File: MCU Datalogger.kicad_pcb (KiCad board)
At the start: 2 copper layers, 0 parts

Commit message: Setup Pcbnew.
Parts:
- added BT1: Battery, Connector_PinHeader_2.54mm:PinHeader_1x02_P2.54mm_Vertical, F.Cu at (227.9, 113.7)
- added C1: 0.1uF, Capacitor_SMD:C_0805_2012Metric, F.Cu at (250.2, 103.4)
- added C2: 22pF, Capacitor_SMD:C_0805_2012Metric, F.Cu at (250.2, 106.4)
- added C3: 22pF, Capacitor_SMD:C_0805_2012Metric, F.Cu at (250.2, 109.4)
- added C4: 0.1uF, Capacitor_SMD:C_0805_2012Metric, F.Cu at (250.2, 112.4)
- added C5: 100nF, Capacitor_SMD:C_0805_2012Metric, F.Cu at (250.2, 115.5)
- added D1: LED, LED_SMD:LED_0805_2012Metric, F.Cu at (254.7, 103.4)
- added D2: LED, LED_SMD:LED_0805_2012Metric, F.Cu at (254.7, 106.5)
- added H1: MountingHole, MountingHole:MountingHole_2.1mm, F.Cu at (228.5, 91.2)
- added H2: MountingHole, MountingHole:MountingHole_2.1mm, F.Cu at (228.5, 97.0)
- added H3: MountingHole, MountingHole:MountingHole_2.1mm, F.Cu at (228.5, 102.7)
- added H4: MountingHole, MountingHole:MountingHole_2.1mm, F.Cu at (228.5, 108.5)
- added J1: Conn_01x04_Pin, Connector_PinHeader_2.54mm:PinHeader_1x04_P2.54mm_Vertical, F.Cu at (265.9, 90.7)
- added J2: Conn_01x09_Pin, Connector_PinHeader_2.54mm:PinHeader_1x09_P2.54mm_Vertical, F.Cu at (261.2, 90.7)
- added J3: Conn_01x04_Pin, Connector_PinHeader_2.54mm:PinHeader_1x04_P2.54mm_Vertical, F.Cu at (270.5, 90.7)
- added J4: Conn_02x03_Odd_Even, Connector_PinHeader_2.54mm:PinHeader_2x03_P2.54mm_Vertical, F.Cu at (265.9, 102.9)
- added R1: 10K, Resistor_SMD:R_0805_2012Metric, F.Cu at (233.6, 89.8)
- added R2: 10K, Resistor_SMD:R_0805_2012Metric, F.Cu at (233.6, 92.8)
- added R3: 4.7K, Resistor_SMD:R_0805_2012Metric, F.Cu at (233.6, 95.7)
- added R4: 4.7K, Resistor_SMD:R_0805_2012Metric, F.Cu at (233.6, 98.7)
- added R5: 330, Resistor_SMD:R_0805_2012Metric, F.Cu at (233.6, 101.6)
- added R6: 10K, Resistor_SMD:R_0805_2012Metric, F.Cu at (233.6, 104.6)
- added R7: 330, Resistor_SMD:R_0805_2012Metric, F.Cu at (233.6, 107.5)
- added U1: 24LC1025, Package_SO:SOIC-8_5.23x5.23mm_P1.27mm, F.Cu at (240.9, 91.8)
- added U2: DS1337S_, Footprints:SOIC127P600X175-8N, F.Cu at (240.9, 116.5)
- added U3: 24LC1025, Package_SO:SOIC-8_5.23x5.23mm_P1.27mm, F.Cu at (240.9, 98.5)
- added U4: ATMEGA328P-AU, Footprints:QFP80P900X900X120-32N, F.Cu at (242.3, 107.6)
- added Y1: 32.768 KHz, Crystal:Crystal_SMD_5032-2Pin_5.0x3.2mm_HandSoldering, F.Cu at (251.2, 90.8)
- added Y2: 16 MHz, Crystal:Crystal_SMD_5032-2Pin_5.0x3.2mm_HandSoldering, F.Cu at (251.2, 95.6)

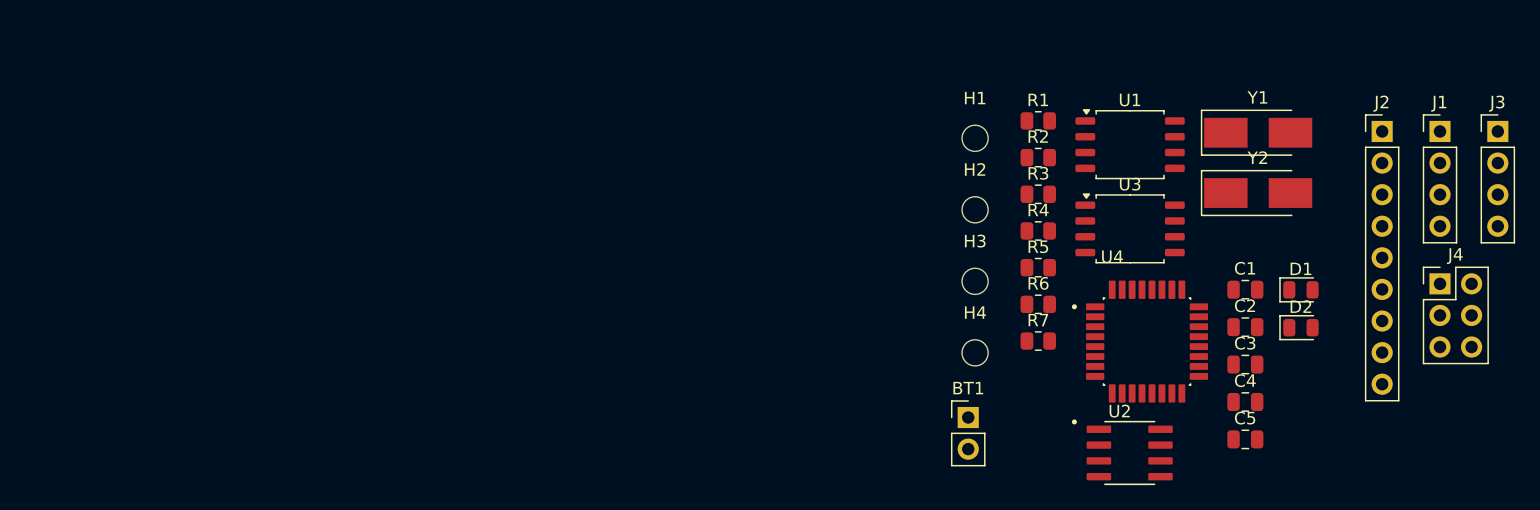
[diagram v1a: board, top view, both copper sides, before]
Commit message: Completed placement of footprints.
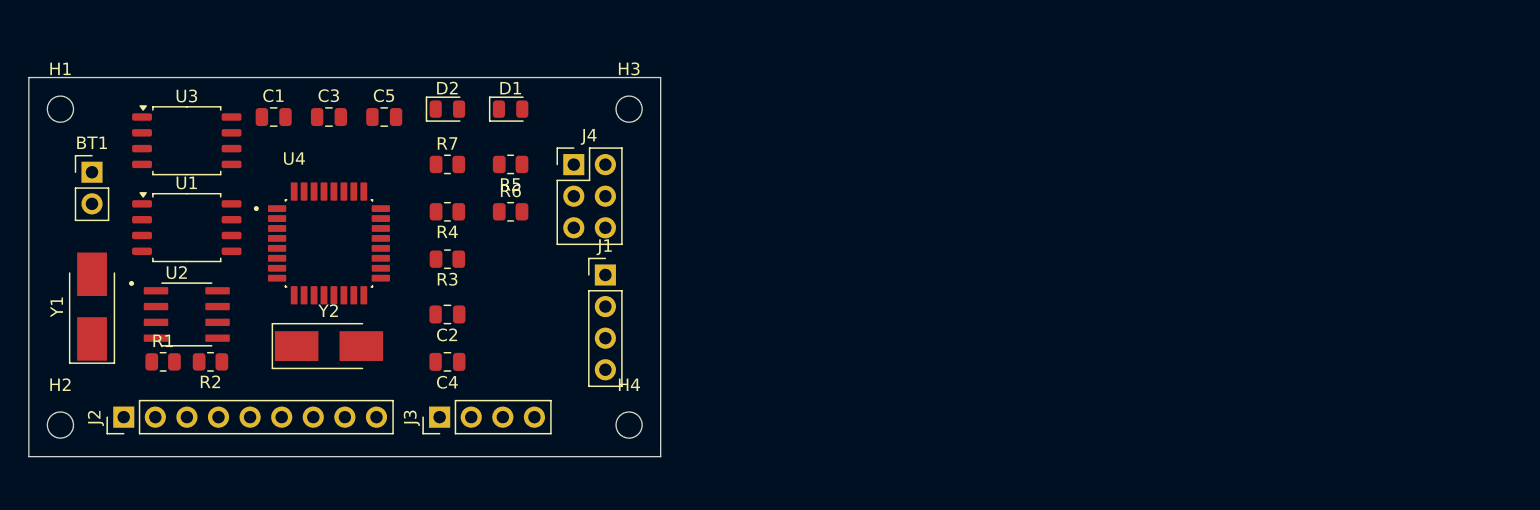
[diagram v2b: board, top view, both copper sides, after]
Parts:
- moved J2 103.8 mm to (160.0, 113.7), turned to 90 degrees
- moved Y1 94.8 mm to (157.5, 104.8), turned to 90 degrees
- moved J3 88.1 mm to (185.4, 113.7), turned to 90 degrees
- moved C1 79.4 mm to (172.1, 89.5)
- moved U2 76.6 mm to (165.1, 105.4)
- moved C3 76.3 mm to (176.5, 89.5)
- moved U3 76.2 mm to (165.1, 91.4)
- moved U1 76.1 mm to (165.1, 98.4)
- moved Y2 75.7 mm to (176.5, 108.0)
- moved H2 75.6 mm to (154.9, 114.3)
- moved C5 73.9 mm to (181.0, 89.5)
- moved H1 73.6 mm to (154.9, 88.9)
- moved BT1 73.2 mm to (157.5, 94.0)
- moved R1 73.0 mm to (163.2, 109.2)
- moved D2 70.8 mm to (186.1, 88.9)
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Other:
- board outline added: 50.8 x 30.5 mm

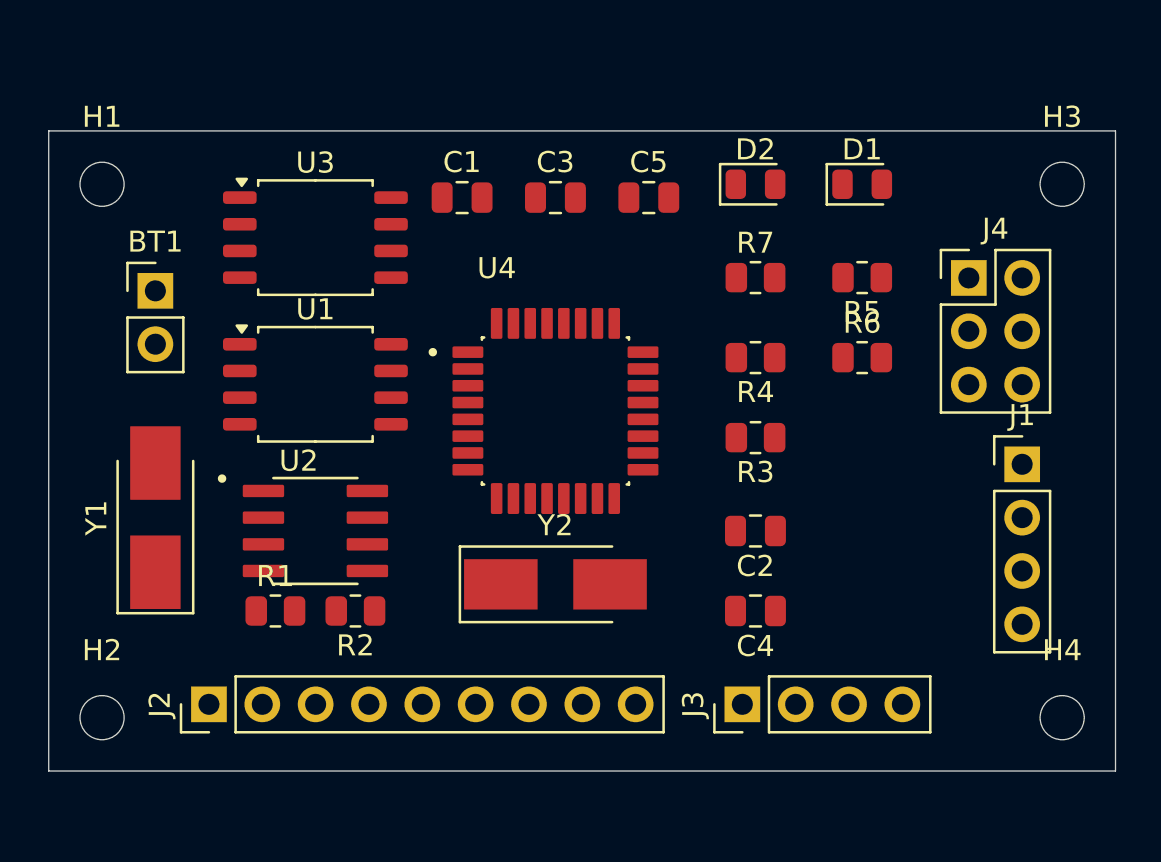
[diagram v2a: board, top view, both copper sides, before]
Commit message: Redesigned board shape.
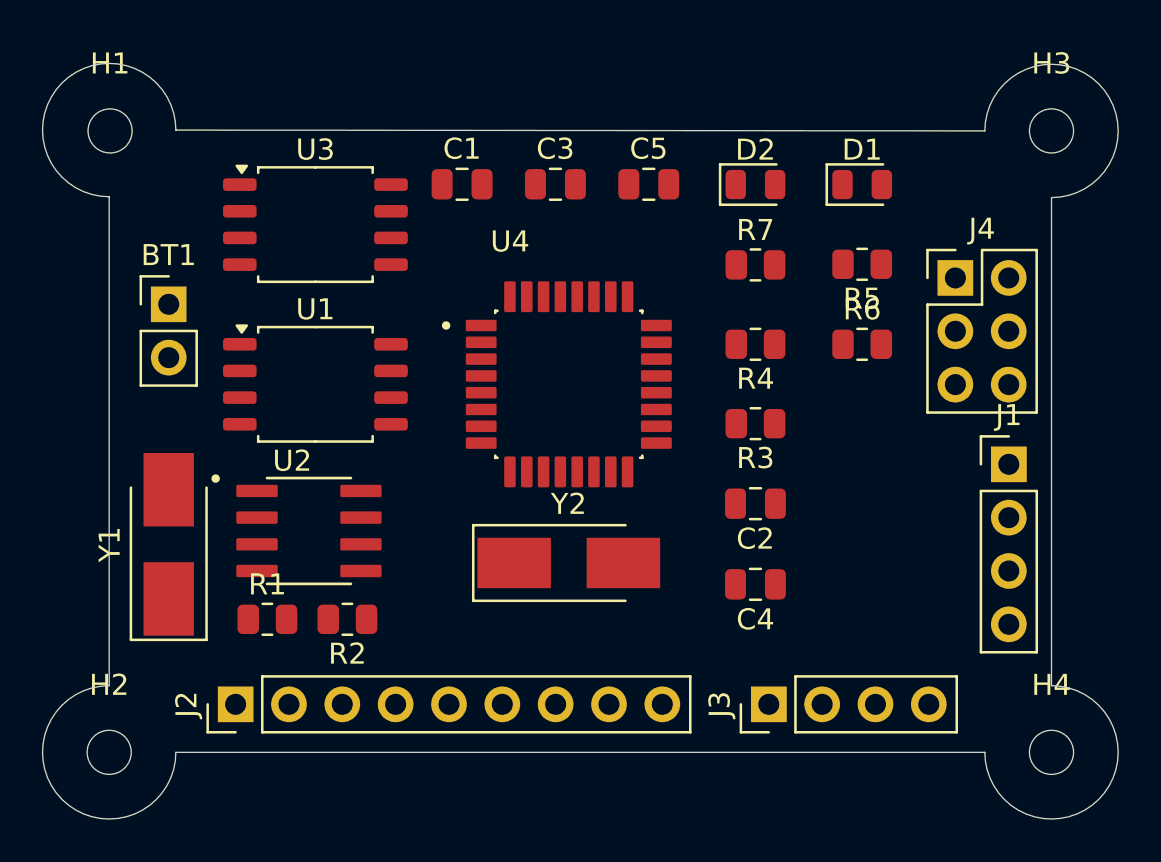
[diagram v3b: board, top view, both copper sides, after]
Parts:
- moved H3 2.59 mm to (200.2, 86.4)
- moved H1 2.57 mm to (155.3, 86.4)
- moved H4 1.73 mm to (200.2, 116.0)
- moved H2 1.69 mm to (155.3, 116.0)
- moved Y1 1.42 mm to (158.1, 106.0)
- moved U4 1.42 mm to (177.2, 98.4)
- moved C2 1.30 mm to (186.1, 104.1)
- moved J2 1.27 mm to (161.3, 113.7)
- moved C4 1.27 mm to (186.1, 108.0)
- moved J3 1.26 mm to (186.7, 113.7)
- moved Y2 1.20 mm to (177.2, 106.9)
- moved BT1 0.90 mm to (158.1, 94.6)
- moved R3 0.67 mm to (186.1, 100.3)
- moved J4 0.64 mm to (195.6, 93.4)
- moved R4 0.64 mm to (186.1, 96.5)
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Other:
- board size 50.8 x 30.5 mm -> 51.2 x 36 mm

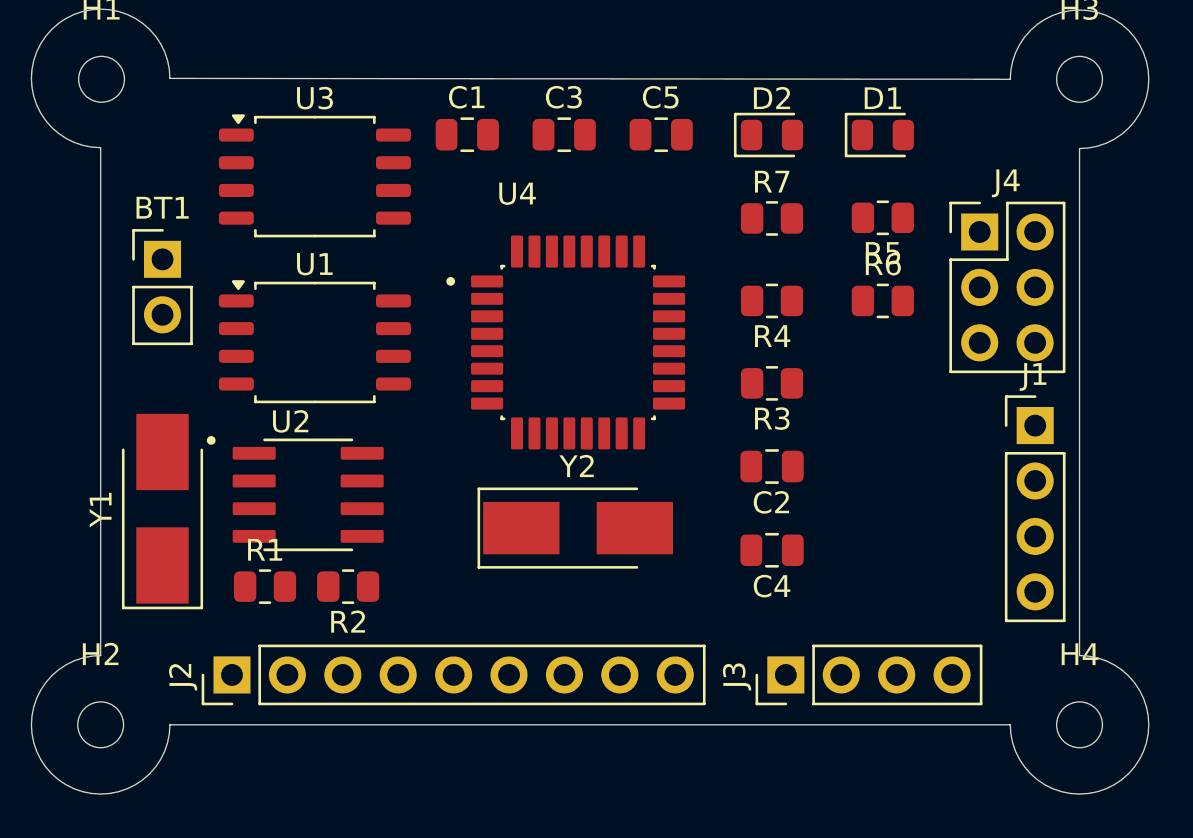
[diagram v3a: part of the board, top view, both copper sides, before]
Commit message: Routing completed (except GND and Vcc).
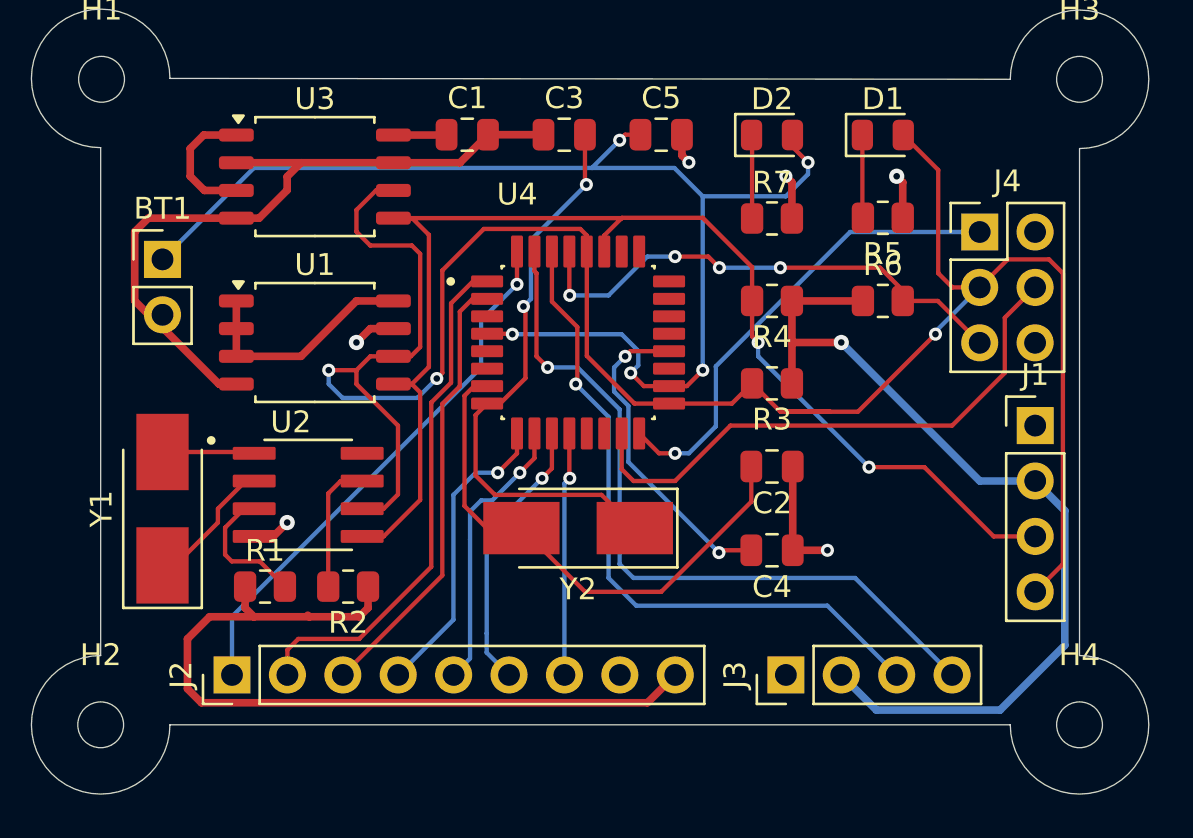
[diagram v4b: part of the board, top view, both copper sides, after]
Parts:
- turned Y2 to 180 degrees
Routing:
- net /SCK: track 0.00 -> 103.3 mm, vias 0 -> 3
- net /Vcc: track 0.00 -> 97.5 mm, vias 0 -> 1
- net /SDA: track 0.00 -> 58.3 mm, vias 0 -> 2
- net Net-(BT1-+): track 0.00 -> 57.5 mm, vias 0 -> 5
- net GND: track 0.00 -> 48.9 mm, vias 0 -> 6
- net /TX: track 0.00 -> 34.1 mm, vias 0 -> 1
- net /RX: track 0.00 -> 31.1 mm, vias 0 -> 1
- net Net-(U4-PB7): track 0.00 -> 26.5 mm, vias 0 -> 2
- net /MOSI: track 0.00 -> 26.0 mm
- net /D2: track 0.00 -> 24.8 mm, vias 0 -> 1
- net Net-(U4-PB6): track 0.00 -> 24.4 mm
- net /D3: track 0.00 -> 23.8 mm
- net /RESET: track 0.00 -> 23.5 mm, vias 0 -> 4
- net /MISO: track 0.00 -> 21.8 mm, vias 0 -> 1
- net /D4: track 0.00 -> 20.4 mm
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
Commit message: Completed routing.
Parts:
- moved H3 0.38 mm to (200.5, 86.4)
- moved H4 0.38 mm to (200.5, 116.0)
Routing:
- net GND: track 48.9 -> 67.7 mm, vias 6 -> 8
- net Net-(U4-PB7): track 26.5 -> 27.5 mm
- net /D3: track 23.8 -> 24.6 mm
- net Net-(BT1-+): track 57.5 -> 58.1 mm
- added copper zone on F.Cu, net /Vcc
- added copper zone on B.Cu, net GND
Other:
- board size 51.2 x 36 mm -> 51.6 x 36 mm

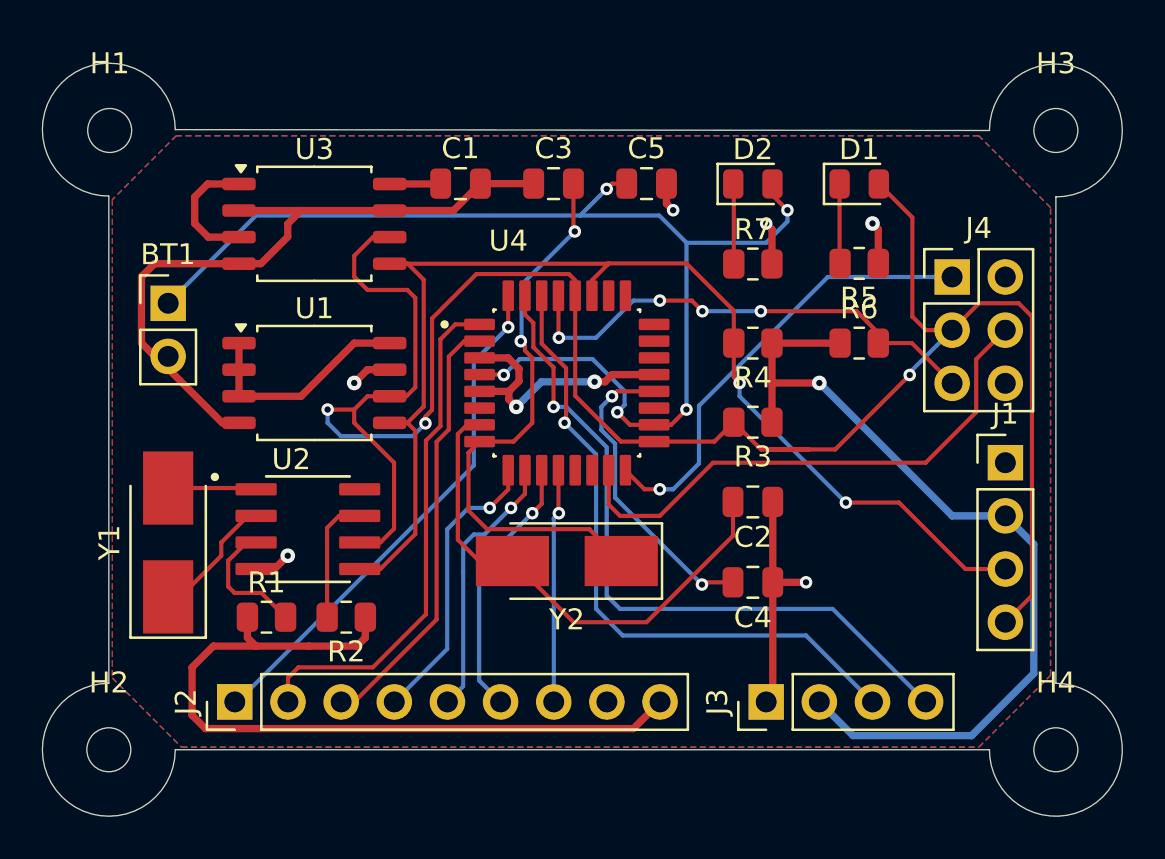
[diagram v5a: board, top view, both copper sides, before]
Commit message: Completed F Silkscreen design.
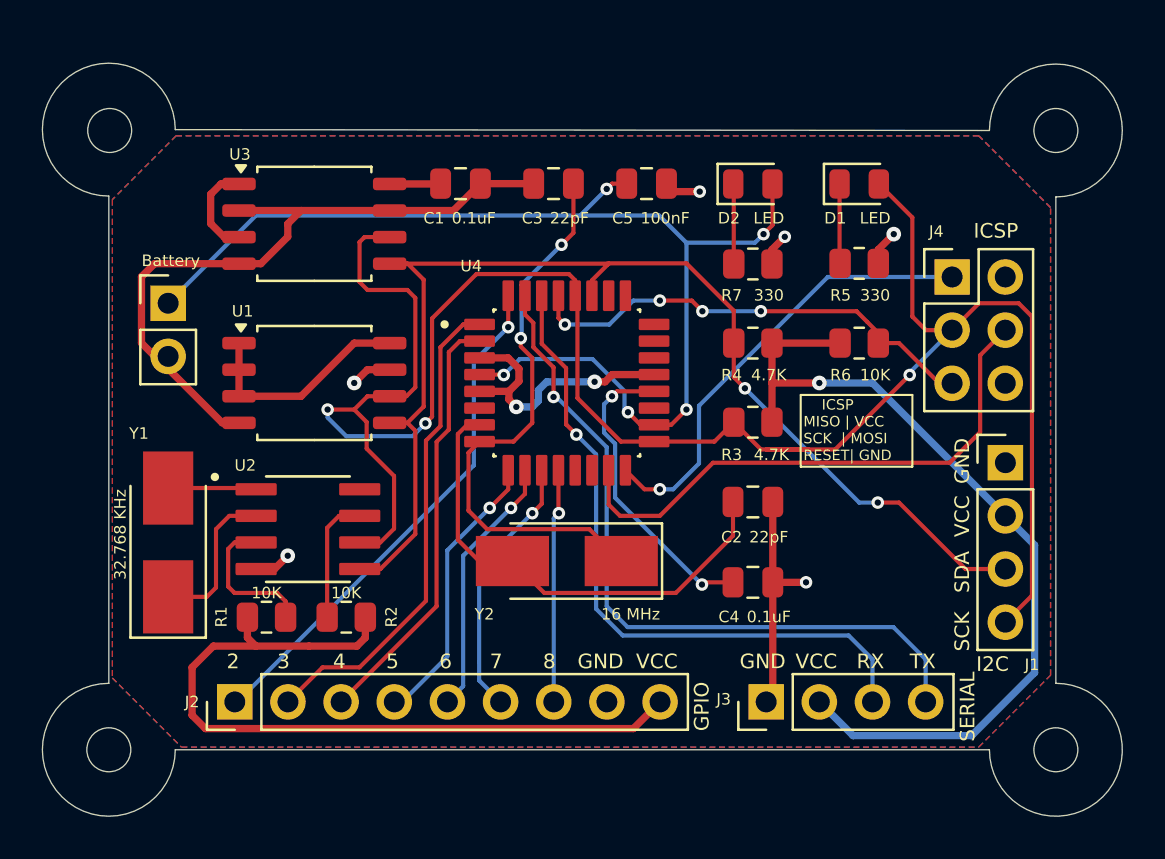
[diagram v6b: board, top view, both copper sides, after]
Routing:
- net Net-(BT1-+): track 58.1 -> 56.6 mm
- net /Vcc: track 97.4 -> 96.0 mm
- net /D3: track 24.6 -> 23.3 mm
- net Net-(U2-X2): track 6.18 -> 7.44 mm
- net /TX: track 33.7 -> 34.9 mm
- net Net-(U4-PB6): track 24.4 -> 23.2 mm
- net /RX: track 31.1 -> 32.3 mm
- net /RESET: track 23.5 -> 22.4 mm
- net Net-(U2-~{INTA}): track 6.28 -> 7.05 mm
- net /MOSI: track 26.0 -> 26.6 mm
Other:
- board text added: "2"
- board text added: "3"
- board text added: "4"
- board text added: "5"
- board text added: "6"
- board text added: "7"
- board text added: "8"
- board text added: "GND"
- board text added: "GPIO"
- board text added: "I2C"
- board text added: "ICSP"
- board text added: "ICSP MISO | VCC SCK | MOSI RESET| GND"
- board text added: "RX"
- board text added: "SCK"
- board text added: "SDA"
- board text added: "SERIAL"
- board text added: "TX"
- board text added: "VCC"

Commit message: Fix outstanding issues.
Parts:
- added REF**: KiCad-Logo2_5mm_SilkScreen, Symbol:KiCad-Logo2_5mm_SilkScreen, B.Cu at (177.4, 90.9)
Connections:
- BT1 pad 1: Net-(BT1-+) -> /Vcc
- C5 pad 1: Net-(BT1-+) -> /Vcc
- D2 pad 2: Net-(BT1-+) -> /Vcc
- U4 pad 18: Net-(BT1-+) -> /Vcc
- U4 pad 4: Net-(BT1-+) -> /Vcc
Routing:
- net /Vcc: track 96.0 -> 153.2 mm, vias 1 -> 6
- net Net-(BT1-+): track 56.6 -> 0.00 mm, vias 5 -> 0
- net GND: track 67.5 -> 68.2 mm
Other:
- board text added: "- 2Mbit EEPROM - RTC - I2C, SPI, GPIOs"
- board text added: "Andrei Enache"
- board text added: "Data logger with ATMega328P"
